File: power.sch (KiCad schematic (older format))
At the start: 26 parts, among them J10 Conn_01x02, J8 Conn_01x02, Q3 DMN63D8LDW, SW3 SW_Push, U3 MCP16331T-E/CH, U4 BTS50080-1TEA, U5 DC_DC_POL

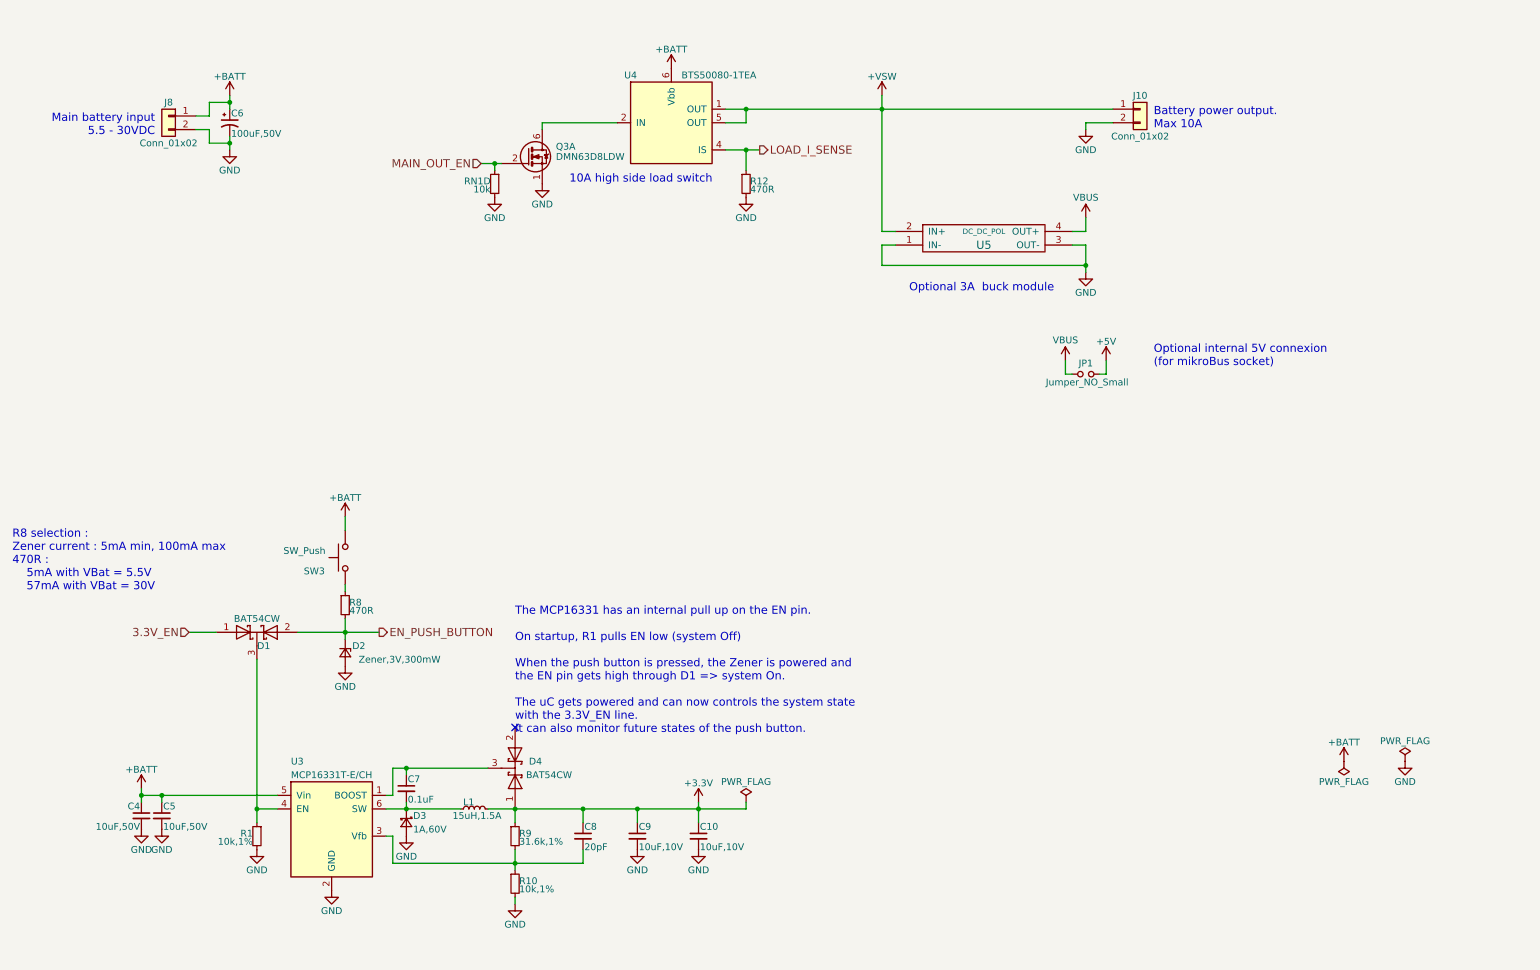
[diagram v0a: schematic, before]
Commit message: v2.0 - audio circuitry on a separate board ; optimized connectors and lots of improvements
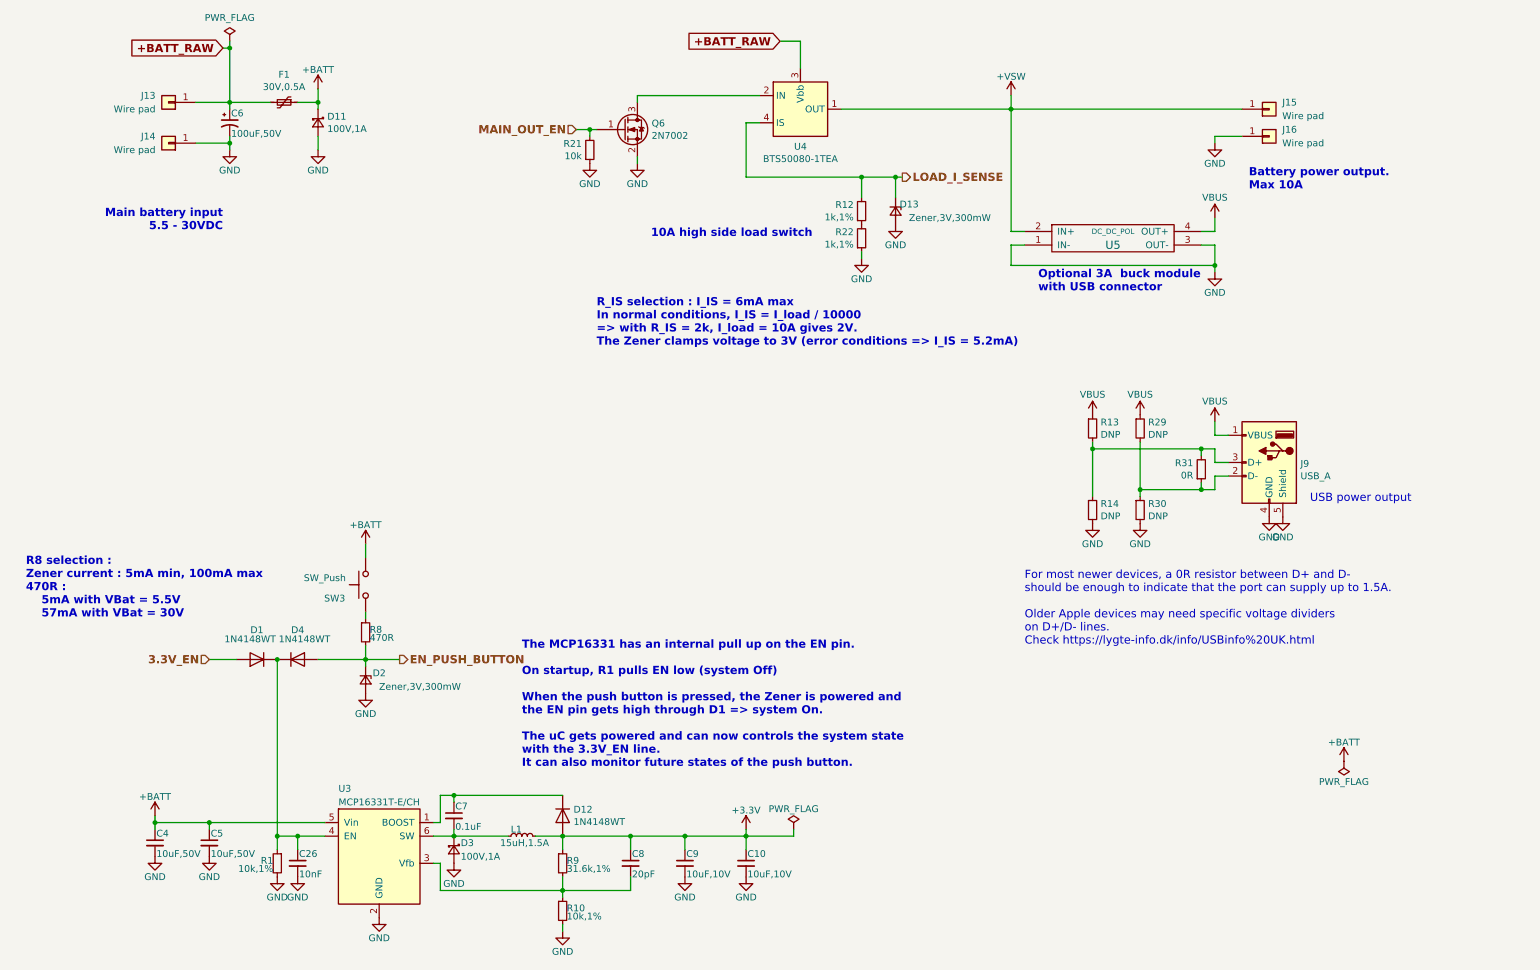
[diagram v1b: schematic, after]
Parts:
- removed D1, D4: BAT54CW, TO_SOT_Packages_SMD:SOT-323_SC-70, symbol KXKM_audio_battery_module-rescue:D_Schottky_x2_KCom_AAK
- removed J10, J8: Conn_01x02, Connectors_Terminal_Blocks:TerminalBlock_Pheonix_PT-3.5mm_2pol, symbol KXKM_audio_battery_module-rescue:Conn_01x02
- removed JP1: Jumper_NO_Small, tom_kicad_lib:Solder_Jumper_2_open, symbol KXKM_audio_battery_module-rescue:Jumper_NO_Small
- removed Q3: DMN63D8LDW, TO_SOT_Packages_SMD:SOT-363_SC-70-6, symbol KXKM_audio_battery_module-rescue:FDG1024NZ
- removed RN1: 10k, Resistors_SMD:R_Array_Convex_4x0402, symbol KXKM_audio_battery_module-rescue:R_Pack04_Unit
- removed U4: BTS50080-1TEA, TO_SOT_Packages_SMD:TO-252-5_TabPin6, symbol KXKM_audio_battery_module-rescue:BTS50080-1TEA
- added C26: 10nF, Capacitor_SMD:C_0603_1608Metric, symbol KXKM_audio_battery_module-rescue:C_Small
- added D1, D12, D4: 1N4148WT, Diode_SMD:D_SOD-523, symbol Diode:1N4148WT
- added D11: 100V,1A, Diode_SMD:D_SMA, symbol Device:D_Schottky_Small
- added D13: Zener,3V,300mW, Diode_SMD:D_SOD-323, symbol KXKM_audio_battery_module-rescue:D_Zener_Small
- added F1: 30V,0.5A, Fuse:Fuse_1812_4532Metric, symbol Device:Polyfuse_Small
- added J13, J14, J15, J16: Wire pad, Connector_Wire:SolderWirePad_1x01_Drill2mm, symbol Connector_Generic:Conn_01x01
- added J9: USB_A, tom_kicad_lib:USB_A_Female, symbol Connector:USB_A
- added Q6: 2N7002, Package_TO_SOT_SMD:SOT-23, symbol Transistor_FET:2N7002
- added R13, R14, R29, R30: DNP, Resistor_SMD:R_0603_1608Metric, symbol Device:R_Small
- added R21: 10k, Resistor_SMD:R_0603_1608Metric, symbol Device:R_Small
- added R22: 1k,1%, Resistor_SMD:R_0603_1608Metric, symbol KXKM_audio_battery_module-rescue:R_Small
- added R31: 0R, Resistor_SMD:R_0603_1608Metric, symbol Device:R_Small
- added U4: BTS50080-1TEA, Package_TO_SOT_SMD:TO-252-4, symbol Power_Management:BTS50080-1TEA
- C10, C9: footprint Capacitors_SMD:C_0805 -> Capacitor_SMD:C_0805_2012Metric
- C4, C5: footprint Capacitors_SMD:C_1206 -> Capacitor_SMD:C_1206_3216Metric
- C6: footprint Capacitors_SMD:CP_Elec_8x10 -> Capacitor_SMD:CP_Elec_8x10
- C7, C8: footprint Capacitors_SMD:C_0603 -> Capacitor_SMD:C_0603_1608Metric
- D2: footprint Diodes_SMD:D_SOD-323 -> Diode_SMD:D_SOD-323
- D3: value 1A,60V -> 100V,1A; footprint Diodes_SMD:D_SOD-123F -> Diode_SMD:D_SMA
- L1: footprint Inductors_SMD:L_7.3x7.3_H4.5 -> Inductor_SMD:L_Taiyo-Yuden_NR-50xx
- R1, R10, R8, R9: footprint Resistors_SMD:R_0603 -> Resistor_SMD:R_0603_1608Metric
- R12: value 470R -> 1k,1%; footprint Resistors_SMD:R_0603 -> Resistor_SMD:R_0603_1608Metric
- U3: footprint TO_SOT_Packages_SMD:SOT-23-6 -> Package_TO_SOT_SMD:SOT-23-6
- U5: footprint tom_kicad_lib:DC_DC_buck_module_Mini360 -> tom_kicad_lib:DC_DC_Buck_module_22x17mm
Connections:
- net +3V3: now also D12.2 (A)
- net +BATT: now also D11.1 (K), F1.1; no longer C6.1
- net +VSW: now also J15.1 (Pin_1), U4.1 (OUT), U4.5 (OUT)
- net 3.3V_EN: now also D1.2 (A)
- net EN_PUSH_BUTTON: now also D4.2 (A)
- net GND: now also C26.2, D11.2 (A), D13.2 (A), J14.1 (Pin_1), J16.1 (Pin_1), J9.4 (GND), J9.5 (Shield), Q6.2 (S), R14.2, R21.1, R22.1, R30.2; no longer R12.2
- net LOAD_I_SENSE: now also R12.2, D13.1 (K), U4.4 (IS); no longer R12.1
- net MAIN_OUT_EN: now also Q6.1 (G), R21.2
- net VBUS: now also J9.1 (VBUS), R13.1, R29.1
- net at C7.1, U3.1 (BOOST): now also D12.1 (K)
- net at R1.1, U3.4 (EN): now also C26.1, D1.1 (K), D4.1 (K)
- new net: R12.1, R22.2
- new net: Q6.3 (D), U4.2 (IN)
- new net: J9.2 (D-), R29.2, R30.1, R31.1
- new net: J9.3 (D+), R13.2, R14.1, R31.2
- new net +BATT_RAW: C6.1, F1.2, J13.1 (Pin_1), U4.3 (Vbb)
- no-connect marks 1 -> 0
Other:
- note added: "For most newer devices, a 0R resistor between D+ and D-\nshould be enough to indicate that the port can supply up to 1.5A.\n\nOlder Apple devices may need specific voltage dividers \non D+/D- lines.\nCheck https://lygte-info.dk/info/USBinfo%20UK.html"
- note added: "Optional 3A buck module \nwith USB connector"
- note added: "R_IS selection : I_IS = 6mA max\nIn normal conditions, I_IS = I_load / 10000\n=> with R_IS = 2k, I_load = 10A gives 2V. \nThe Zener clamps voltage to 3V (error conditions => I_IS = 5.2mA)"
- note added: "USB power output"
- note removed: "Optional 3A buck module"
- note removed: "Optional internal 5V connexion \n(for mikroBus socket)"
- moved on the sheet: C10, C4, C5, C7, C8, C9, D2, D3, L1, R1, R10, R12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
